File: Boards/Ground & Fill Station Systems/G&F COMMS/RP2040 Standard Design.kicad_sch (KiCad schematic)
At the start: 40 parts, among them J1 BM03B-SRSS-TBLFSN, J4 DX07S016JA1R1500, U1 RP2040, U2 W25Q128JVSIQ TR, U5 ESD7L5.0DT5G, U6 ST1L05APU33R

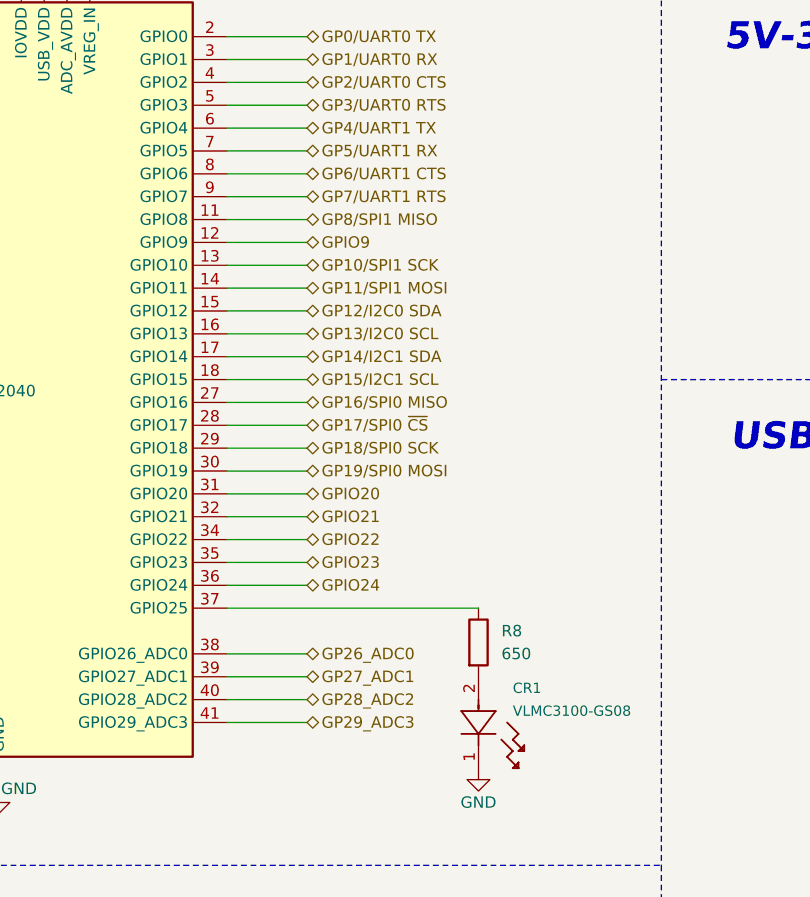
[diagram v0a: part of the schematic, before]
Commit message: Led driver circuit correction & RF FEM implementation
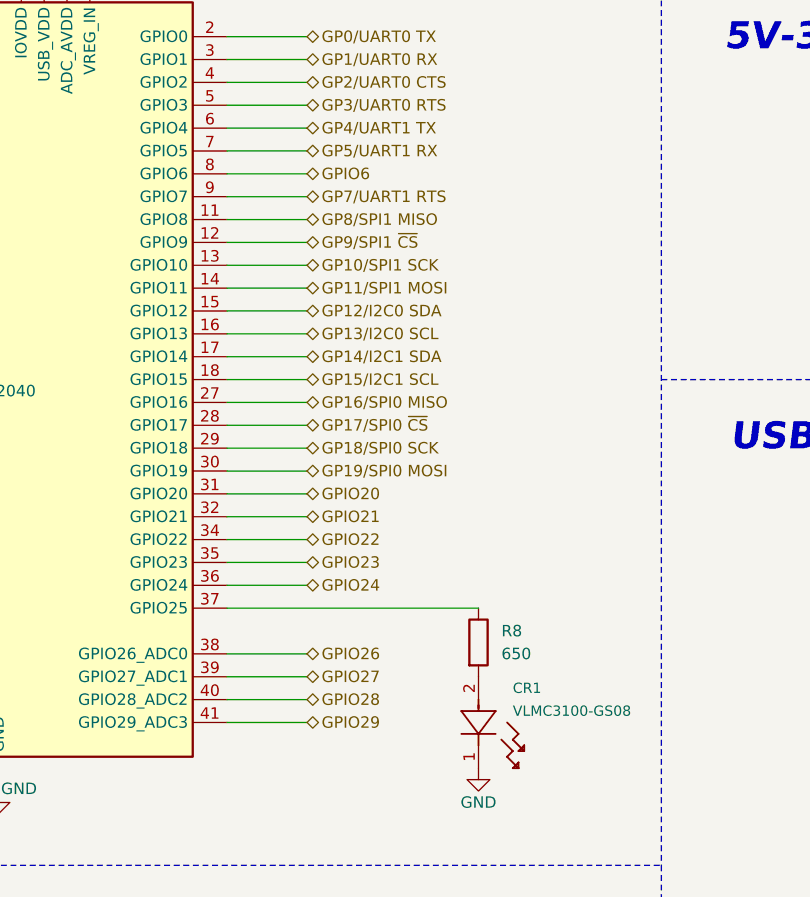
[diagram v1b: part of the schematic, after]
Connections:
- net GP26_ADC0 renamed GPIO26
- net GP27_ADC1 renamed GPIO27
- net GP28_ADC2 renamed GPIO28
- net GP29_ADC3 renamed GPIO29
- net GP6/UART1 CTS renamed GPIO6
- net GPIO9 renamed GP9/SPI1 ~{CS}
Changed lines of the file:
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@@
 		)
 	)
-	(hierarchical_label "GPIO9"
+	(hierarchical_label "GP9{slash}SPI1 ~{CS}"
 		(shape bidirectional)
 		(at 107.95 93.345 0)
@@
 		)
 	)
-	(hierarchical_label "GP29_ADC3"
+	(hierarchical_label "GPIO29"
 		(shape bidirectional)
 		(at 107.95 146.685 0)
@@
 		)
 	)
-	(hierarchical_label "GP6{slash}UART1 CTS"
+	(hierarchical_label "GPIO6"
 		(shape bidirectional)
 		(at 107.95 85.725 0)
@@
 		)
 	)
-	(hierarchical_label "GP27_ADC1"
+	(hierarchical_label "GPIO27"
 		(shape bidirectional)
 		(at 107.95 141.605 0)
@@
 		)
 	)
-	(hierarchical_label "GP26_ADC0"
+	(hierarchical_label "GPIO26"
 		(shape bidirectional)
 		(at 107.95 139.065 0)
@@
 		)
 	)
-	(hierarchical_label "GP28_ADC2"
+	(hierarchical_label "GPIO28"
 		(shape bidirectional)
 		(at 107.95 144.145 0)

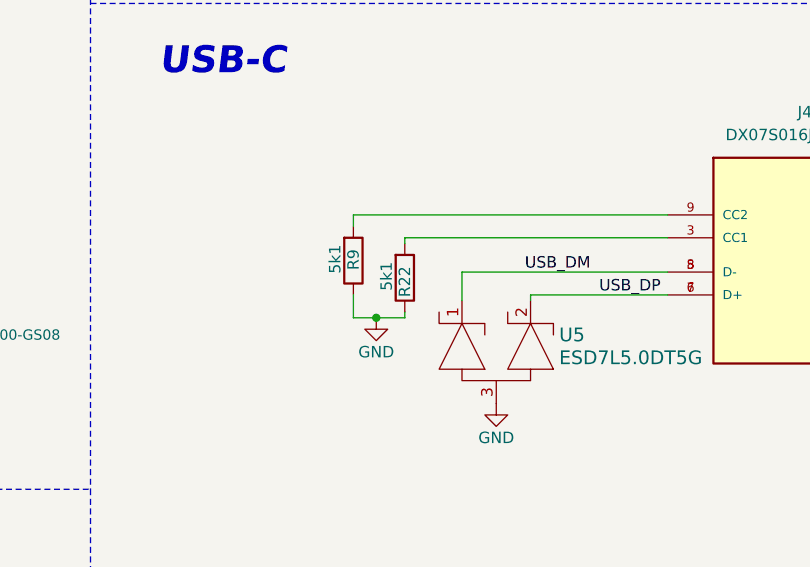
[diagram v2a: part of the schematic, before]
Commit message: Final DCDC design and update part1 COMM board
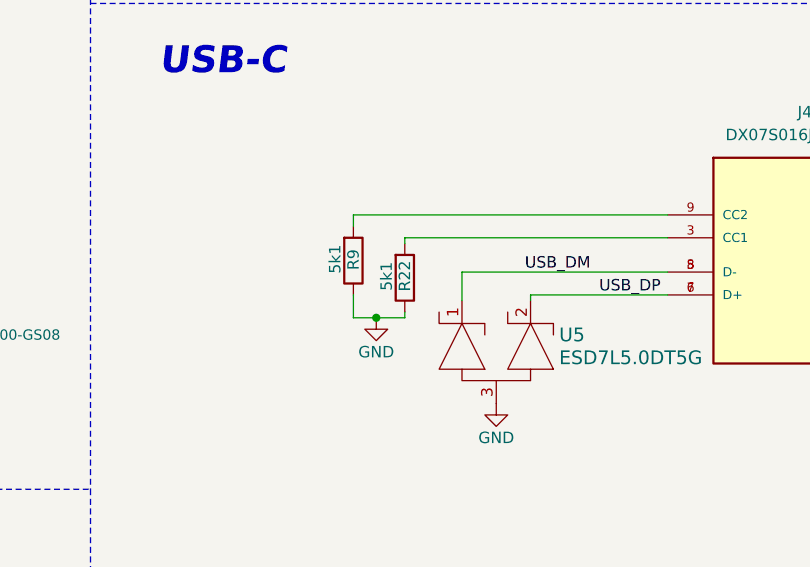
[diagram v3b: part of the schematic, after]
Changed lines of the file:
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@@
 	(label "MCU QSPI_SS"
 		(at 162.56 45.72 0)
-		(fields_autoplaced yes)
 		(effects
 			(font
@@
 	(label "MCU QSPI_SD1"
 		(at 162.56 48.26 0)
-		(fields_autoplaced yes)
 		(effects
 			(font
@@
 	(label "USB_DP"
 		(at 203.835 140.97 0)
-		(fields_autoplaced yes)
 		(effects
 			(font
@@
 	(label "USB_DM"
 		(at 28.575 80.645 0)
-		(fields_autoplaced yes)
 		(effects
 			(font
@@
 	(label "USB_DP"
 		(at 28.575 78.105 0)
-		(fields_autoplaced yes)
 		(effects
 			(font
@@
 	(label "MCU QSPI_SCLK"
 		(at 33.02 103.505 0)
-		(fields_autoplaced yes)
 		(effects
 			(font
@@
 	(label "MCU QSPI_SD0"
 		(at 33.02 93.345 0)
-		(fields_autoplaced yes)
 		(effects
 			(font
@@
 	(label "MCU QSPI_SCLK"
 		(at 281.305 50.8 180)
-		(fields_autoplaced yes)
 		(effects
 			(font
@@
 	(label "MCU QSPI_SD3"
 		(at 281.305 48.26 180)
-		(fields_autoplaced yes)
 		(effects
 			(font
@@
 	(label "~{USB_BOOT}"
 		(at 170.18 34.29 0)
-		(fields_autoplaced yes)
 		(effects
 			(font
@@
 	(label "MCU QSPI_SD1"
 		(at 33.02 95.885 0)
-		(fields_autoplaced yes)
 		(effects
 			(font
@@
 	(label "~{RST}"
 		(at 42.545 53.34 0)
-		(fields_autoplaced yes)
 		(effects
 			(font
@@
 	(label "MCU QSPI_SD3"
 		(at 33.02 100.965 0)
-		(fields_autoplaced yes)
 		(effects
 			(font
@@
 	(label "MCU QSPI_SD0"
 		(at 281.305 53.34 180)
-		(fields_autoplaced yes)
 		(effects
 			(font
@@
 	(label "MCU QSPI_SD2"
 		(at 33.02 98.425 0)
-		(fields_autoplaced yes)
 		(effects
 			(font
@@
 	(label "USB_DM"
 		(at 195.58 138.43 0)
-		(fields_autoplaced yes)
 		(effects
 			(font
@@
 	(label "MCU QSPI_SS"
 		(at 33.02 88.265 0)
-		(fields_autoplaced yes)
 		(effects
 			(font
@@
 	(label "MCU QSPI_SD2"
 		(at 162.56 50.8 0)
-		(fields_autoplaced yes)
 		(effects
 			(font
@@
 		(shape bidirectional)
 		(at 107.95 126.365 0)
-		(fields_autoplaced yes)
 		(effects
 			(font
@@
 		(shape bidirectional)
 		(at 107.95 100.965 0)
-		(fields_autoplaced yes)
 		(effects
 			(font
@@
 		(shape bidirectional)
 		(at 107.95 75.565 0)
-		(fields_autoplaced yes)
 		(effects
 			(font
@@
 		(shape bidirectional)
 		(at 107.95 131.445 0)
-		(fields_autoplaced yes)
 		(effects
 			(font
@@
 		(shape bidirectional)
 		(at 107.95 121.285 0)
-		(fields_autoplaced yes)
 		(effects
 			(font
@@
 		(shape bidirectional)
 		(at 107.95 116.205 0)
-		(fields_autoplaced yes)
 		(effects
 			(font
@@
 		(shape bidirectional)
 		(at 107.95 93.345 0)
-		(fields_autoplaced yes)
 		(effects
 			(font
@@
 		(shape bidirectional)
 		(at 107.95 98.425 0)
-		(fields_autoplaced yes)
 		(effects
 			(font
@@
 		(shape bidirectional)
 		(at 107.95 70.485 0)
-		(fields_autoplaced yes)
 		(effects
 			(font
@@
 		(shape bidirectional)
 		(at 107.95 78.105 0)
-		(fields_autoplaced yes)
 		(effects
 			(font
@@
 		(shape bidirectional)
 		(at 107.95 95.885 0)
-		(fields_autoplaced yes)
 		(effects
 			(font
@@
 		(shape bidirectional)
 		(at 107.95 106.045 0)
-		(fields_autoplaced yes)
 		(effects
 			(font
@@
 		(shape bidirectional)
 		(at 107.95 103.505 0)
-		(fields_autoplaced yes)
 		(effects
 			(font
@@
 		(shape bidirectional)
 		(at 107.95 118.745 0)
-		(fields_autoplaced yes)
 		(effects
 			(font
@@
 		(shape bidirectional)
 		(at 107.95 73.025 0)
-		(fields_autoplaced yes)
 		(effects
 			(font
@@
 		(shape bidirectional)
 		(at 107.95 146.685 0)
-		(fields_autoplaced yes)
 		(effects
 			(font
@@
 		(shape input)
 		(at 255.905 126.365 90)
-		(fields_autoplaced yes)
 		(effects
 			(font
@@
 		(shape bidirectional)
 		(at 107.95 85.725 0)
-		(fields_autoplaced yes)
 		(effects
 			(font
@@
 		(shape bidirectional)
 		(at 107.95 123.825 0)
-		(fields_autoplaced yes)
 		(effects
 			(font
@@
 		(shape bidirectional)
 		(at 107.95 111.125 0)
-		(fields_autoplaced yes)
 		(effects
 			(font
@@
 		(shape bidirectional)
 		(at 107.95 141.605 0)
-		(fields_autoplaced yes)
 		(effects
 			(font
@@
 		(shape bidirectional)
 		(at 107.95 113.665 0)
-		(fields_autoplaced yes)
 		(effects
 			(font
@@
 		(shape bidirectional)
 		(at 107.95 88.265 0)
-		(fields_autoplaced yes)
 		(effects
 			(font
@@
 		(shape input)
 		(at 178.435 83.82 90)
-		(fields_autoplaced yes)
 		(effects
 			(font
@@
 		(shape bidirectional)
 		(at 107.95 80.645 0)
-		(fields_autoplaced yes)
 		(effects
 			(font
@@
 		(shape bidirectional)
 		(at 107.95 108.585 0)
-		(fields_autoplaced yes)
 		(effects
 			(font
@@
 		(shape bidirectional)
 		(at 107.95 128.905 0)
-		(fields_autoplaced yes)
 		(effects
 			(font
@@
 		(shape bidirectional)
 		(at 107.95 83.185 0)
-		(fields_autoplaced yes)
 		(effects
 			(font
@@
 		(shape bidirectional)
 		(at 107.95 139.065 0)
-		(fields_autoplaced yes)
 		(effects
 			(font
@@
 		(shape bidirectional)
 		(at 107.95 90.805 0)
-		(fields_autoplaced yes)
 		(effects
 			(font
@@
 		(shape bidirectional)
 		(at 107.95 144.145 0)
-		(fields_autoplaced yes)
 		(effects
 			(font
@@
 		(dnp no)
 		(property "Reference" "R22"
-			(at 182.245 137.795 90)
-			(effects
-				(font
+			(at 182.245 137.16 90)
+			(effects
+				(font

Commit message: Communication boards update
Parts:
- renumbered C1 to C52, C2 to C53, C3 to C54, C4 to C55, C5 to C56, C6 to C57, C7 to C58, C8 to C59, C9 to C60, C10 to C61, C11 to C62, C12 to C63, C13 to C64, C14 to C65, C15 to C66, C16 to C67, C17 to C68, C18 to C69, CR1 to CR9, D1 to D3, J1 to J12, J4 to J13, R1 to R38, R2 to R39, R3 to R40, R4 to R41, R5 to R42, R6 to R43, R7 to R44, R8 to R45, R9 to R46, R19 to R47, R22 to R48, S3 to S6, S4 to S7, U1 to U13, U2 to U14, U5 to U15, U6 to U16, XTAL1 to XTAL4
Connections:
- net GP12/I2C0 SDA renamed GPIO12
- net GP13/I2C0 SCL renamed GP13/SPI1 ~{CS}
- net GP7/UART1 RTS renamed GPIO7

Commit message: System update
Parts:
- removed S6, S7: TL3305CF160QG, TL3305CF160QG:SW_TL3305CF160QG, symbol TL3305CF160QG:TL3305CF160QG
- added S1, S3: TL1017AABF160QG, TL1017AABF160QG, symbol TL1017AABF160QG:TL1017AABF160QG
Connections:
- net GND: now also S1.1 (COM), S1.G1, S3.1 (COM), S3.G1
- net ~{RST}: now also S1.2 (NO)
- net ~{USB_BOOT}: now also S3.2 (NO)
- no-connect marks 8 -> 4

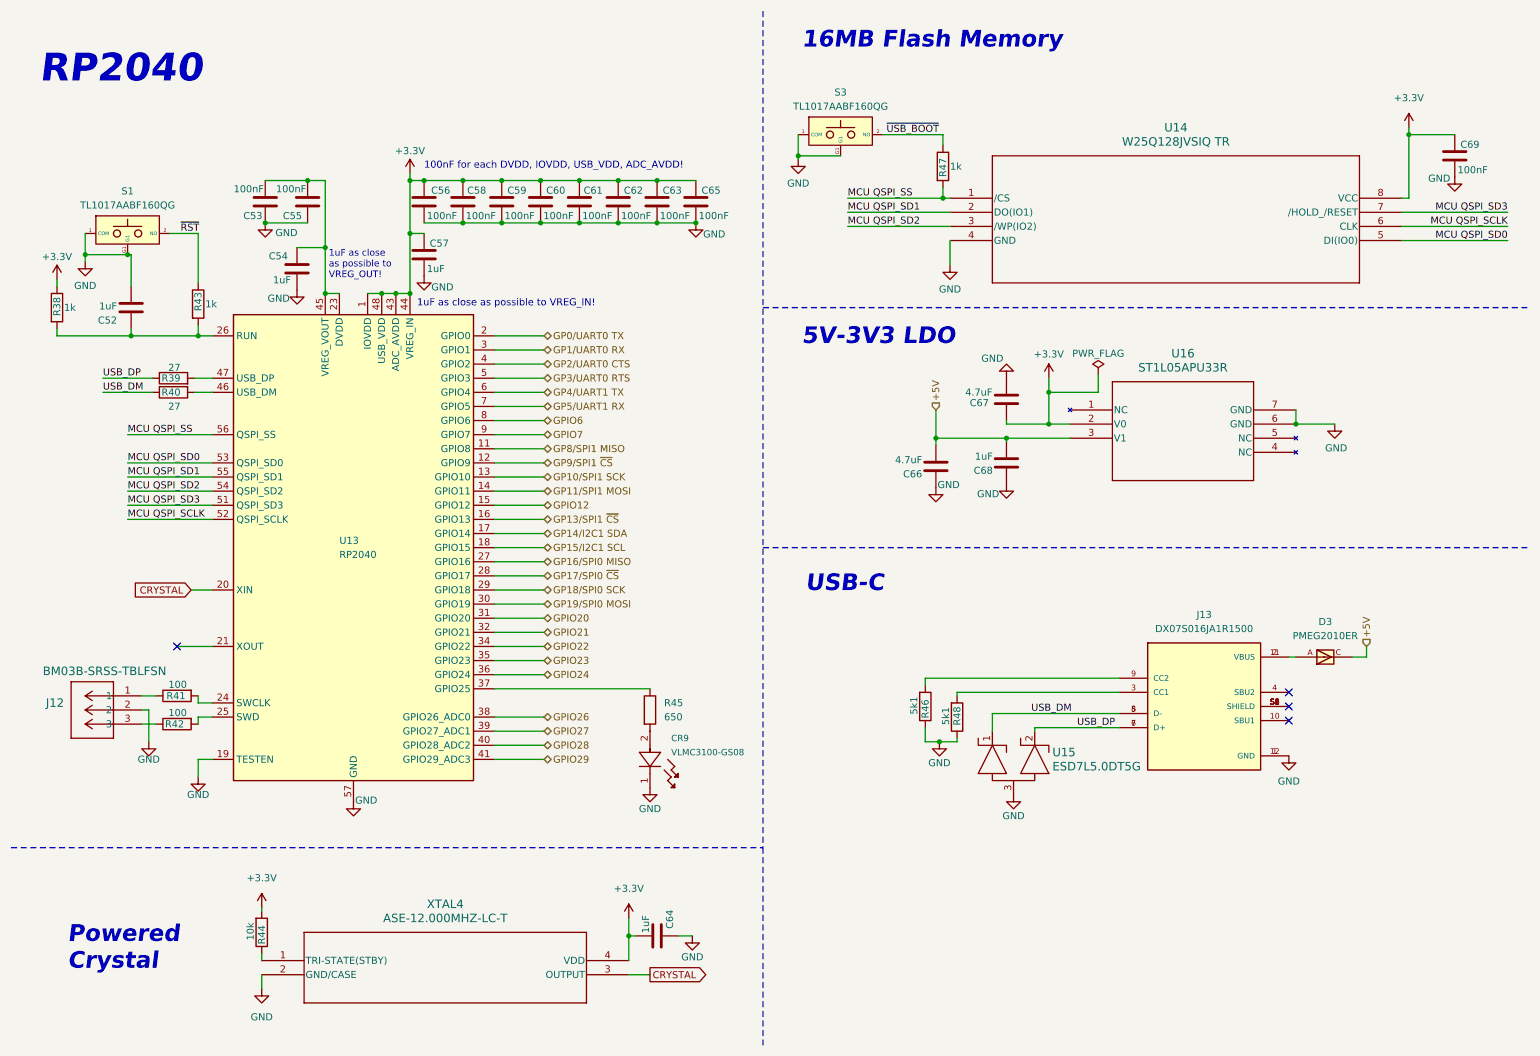
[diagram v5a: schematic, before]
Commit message: USB-C PD update and schematic corrections
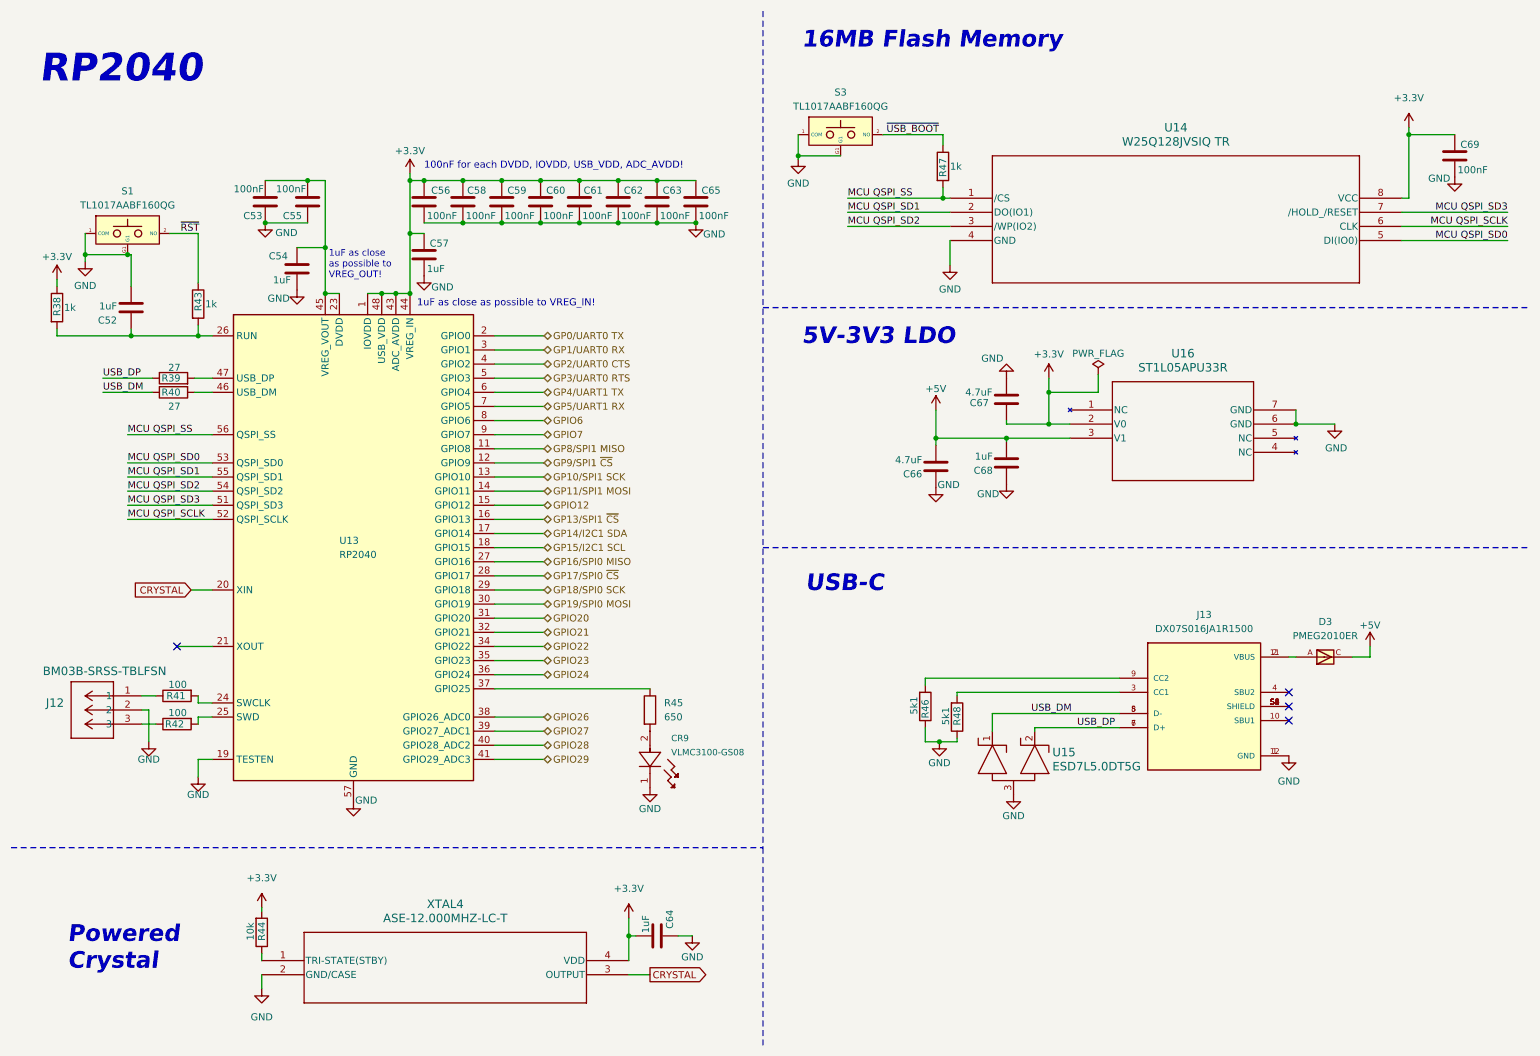
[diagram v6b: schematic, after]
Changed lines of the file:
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@@
 	(wire
 		(pts
-			(xy 255.905 128.27) (xy 253.365 128.27)
+			(xy 256.54 128.27) (xy 253.365 128.27)
 		)
 		(stroke
@@
 	(wire
 		(pts
-			(xy 255.905 126.365) (xy 255.905 128.27)
+			(xy 256.54 126.365) (xy 256.54 128.27)
 		)
 		(stroke
@@
 		)
 	)
-	(hierarchical_label "+5V"
-		(shape input)
-		(at 255.905 126.365 90)
-		(effects
-			(font
-				(size 1.27 1.27)
-			)
-			(justify left)
-		)
-	)
 	(hierarchical_label "GPIO6"
 		(shape bidirectional)
@@
 		)
 	)
-	(hierarchical_label "+5V"
-		(shape input)
-		(at 178.435 83.82 90)
-		(effects
-			(font
-				(size 1.27 1.27)
-			)
-			(justify left)
-		)
-	)
 	(hierarchical_label "GP4{slash}UART1 TX"
 		(shape bidirectional)
@@
 	)
 	(symbol
+		(lib_id "power:+5V")
+		(at 256.54 126.365 0)
+		(unit 1)
+		(exclude_from_sim no)
+		(in_bom yes)
+		(on_board yes)
+		(dnp no)
+		(property "Reference" "#PWR05"
+			(at 256.54 130.175 0)
+			(effects
+				(font
+					(size 1.27 1.27)
+				)
+				(hide yes)
+			)
+		)
+		(property "Value" "+5V"
+			(at 256.54 122.555 0)
+			(effects
+				(font
+					(size 1.27 1.27)
+				)
+			)
+		)
+		(property "Footprint" ""
+			(at 256.54 126.365 0)
+			(effects
+				(font
+					(size 1.27 1.27)
+				)
+				(hide yes)
+			)
+		)
+		(property "Datasheet" ""
+			(at 256.54 126.365 0)
+			(effects
+				(font
+					(size 1.27 1.27)
+				)
+				(hide yes)
+			)
+		)
+		(property "Description" "Power symbol creates a global label with name \"+5V\""
+			(at 256.54 126.365 0)
+			(effects
+				(font
+					(size 1.27 1.27)
+				)
+				(hide yes)
+			)
+		)
+		(pin "1"
+		)
+		(instances
+			(project "G&F COMMS"
+				(path "/169b1789-9bea-4709-830d-1c7983087293/c39ae272-8c0d-42d2-a73f-6dde4bfe6a15"
+					(reference "#PWR05")
+					(unit 1)
+				)
+			)
+		)
+	)
+	(symbol
 		(lib_id "power:GND")
 		(at 179.07 143.51 0)
@@
 		(dnp no)
 		(property "Reference" "R44"
-			(at 57.15 176.53 90)
+			(at 57.15 175.895 90)
 			(effects
 				(font
@@
 					(unit 1)
 				)
+			)
+		)
+	)
+	(symbol
+		(lib_id "power:+5V")
+		(at 178.435 83.82 0)
+		(unit 1)
+		(exclude_from_sim no)
+		(in_bom yes)
+		(on_board yes)
+		(dnp no)
+		(property "Reference" "#PWR06"
+			(at 178.435 87.63 0)
+			(effects
+				(font
+					(size 1.27 1.27)
+				)
+				(hide yes)
+			)
+		)
+		(property "Value" "+5V"
+			(at 178.435 80.01 0)
+			(effects
+				(font
+					(size 1.27 1.27)
+				)
+			)
+		)
+		(property "Footprint" ""
+			(at 178.435 83.82 0)
+			(effects
+				(font
+					(size 1.27 1.27)
+				)
+				(hide yes)
+			)
+		)
+		(property "Datasheet" ""
+			(at 178.435 83.82 0)
+			(effects
+				(font
+					(size 1.27 1.27)
+				)
+				(hide yes)
+			)
+		)
+		(property "Description" "Power symbol creates a global label with name \"+5V\""
+			(at 178.435 83.82 0)
+			(effects
+				(font
+					(size 1.27 1.27)
+				)
+				(hide yes)
+			)
+		)
+		(pin "1"
+		)
+		(instances
+			(project "G&F COMMS"
+				(path "/169b1789-9bea-4709-830d-1c7983087293/c39ae272-8c0d-42d2-a73f-6dde4bfe6a15"
+					(reference "#PWR06")
+					(unit 1)
+				)
